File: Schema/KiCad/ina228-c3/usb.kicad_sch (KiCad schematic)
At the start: 17 parts, among them U5 CP2102N-Axx-xQFN28, U6 CA-IS3741HW, U7 USBLC6-2P6

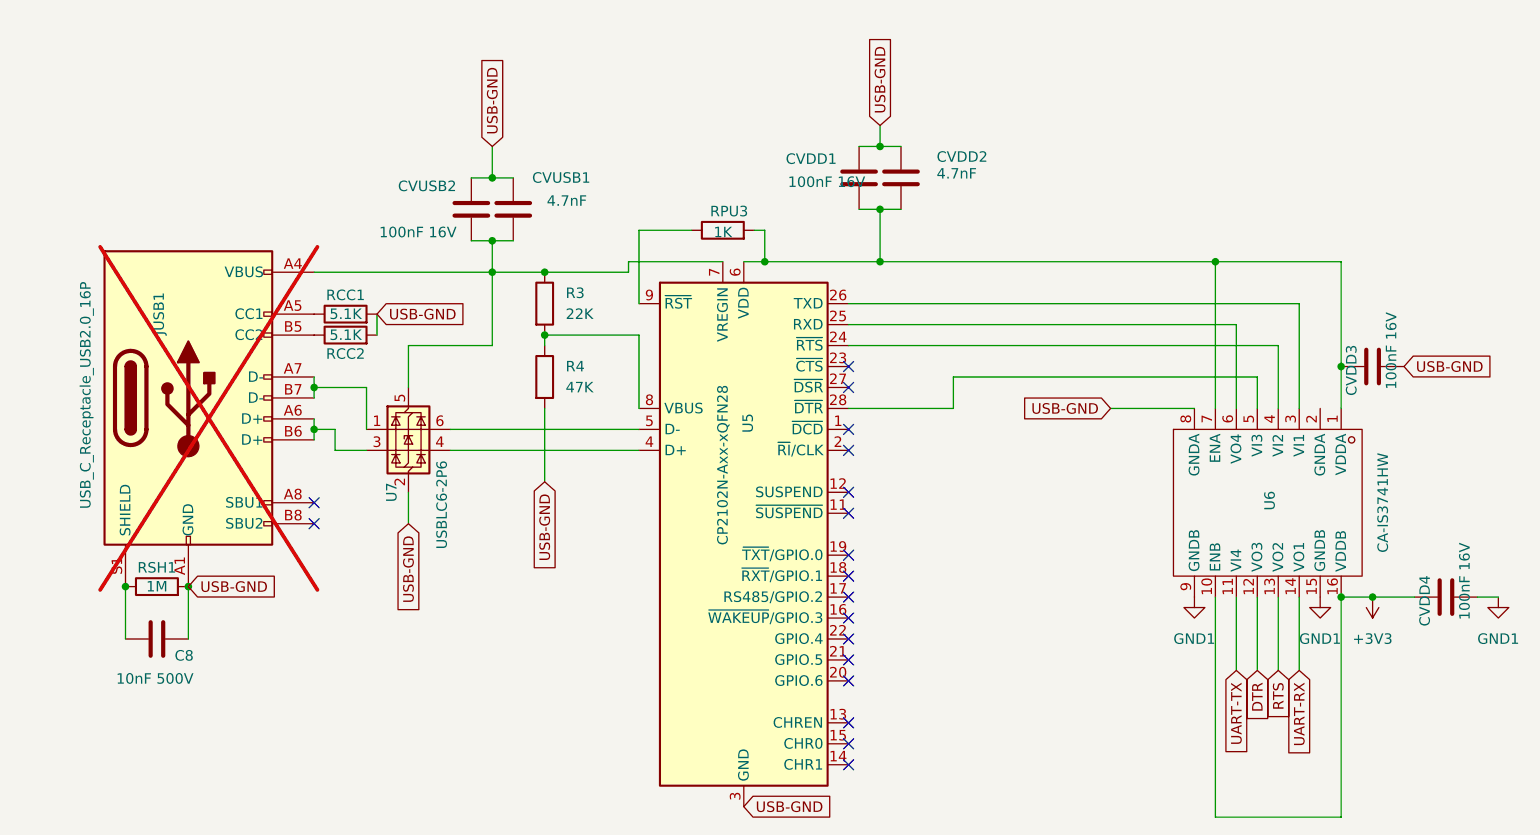
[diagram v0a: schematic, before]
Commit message: Remove usb2uart chip, making the design simpler (but probably more expensive.)
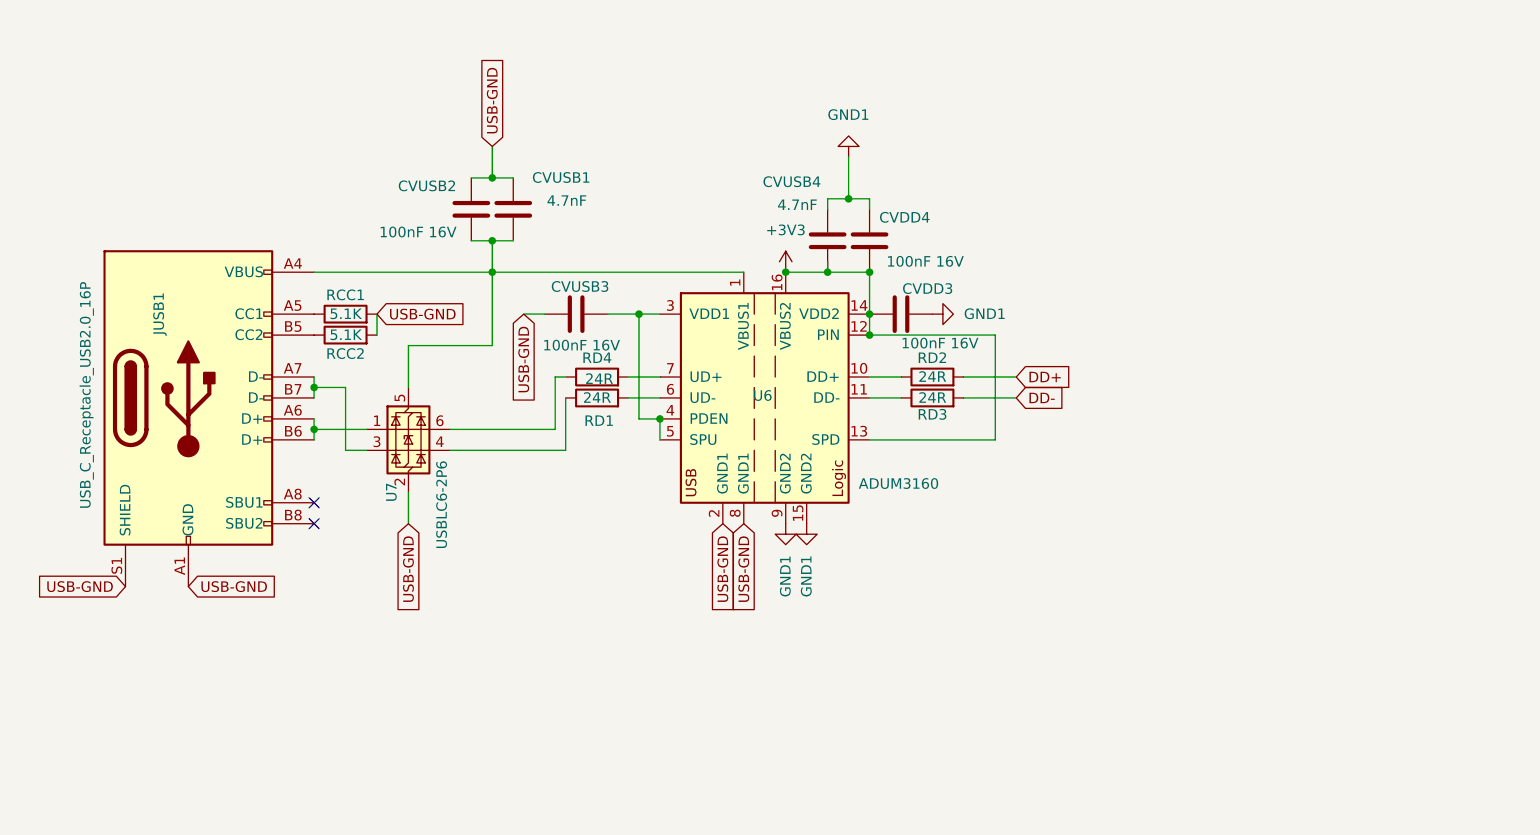
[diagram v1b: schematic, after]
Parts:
- removed C8: 10nF 500V, Capacitor_SMD:C_1206_3216Metric, symbol Device:C
- removed CVDD1: 100nF 16V, Capacitor_SMD:C_0603_1608Metric, symbol Device:C
- removed CVDD2: 4.7nF, Capacitor_SMD:C_0805_2012Metric, symbol Device:C
- removed R3: 22K, Resistor_SMD:R_0603_1608Metric, symbol Device:R
- removed R4: 47K, Resistor_SMD:R_0603_1608Metric, symbol Device:R
- removed RPU3: 1K, Resistor_SMD:R_0603_1608Metric, symbol Device:R
- removed RSH1: 1M, Resistor_SMD:R_0603_1608Metric, symbol Device:R
- removed U5: CP2102N-Axx-xQFN28, Package_DFN_QFN:QFN-28-1EP_5x5mm_P0.5mm_EP3.35x3.35mm, symbol Interface_USB:CP2102N-Axx-xQFN28
- added CVUSB3: 100nF 16V, Capacitor_SMD:C_0603_1608Metric, symbol Device:C
- added CVUSB4: 4.7nF, Capacitor_SMD:C_0805_2012Metric, symbol Device:C
- added RD1, RD2, RD3, RD4: 24R, Resistor_SMD:R_0603_1608Metric, symbol Device:R
- JUSB1: footprint easyeda:USB-C-SMD_TYPE-C16PIN -> Connector_USB:USB_C_Receptacle_Palconn_UTC16-G; now fitted
- U6: value CA-IS3741HW -> ADUM3160; symbol ProLib_pcs_2026-02-13:CA-IS3741HW -> Interface_USB:ADUM3160; LCSC C428890 -> C284149; LCSC Part Name CA-IS374x 高速四通道数字隔离器 -> (none); Supplier Part C428890 -> (none)
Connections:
- net DTR is gone; now on net +3V3: U6.12 (PIN)
- net RTS is gone; now on net +3V3: U6.13 (SPD)
- net UART-RX is gone; now on net +3V3: U6.14 (VDD2)
- net +3V3: now also CVDD3.1, CVUSB4.2; no longer U6.10 (ENB)
- net GND1: now also CVDD3.2, CVUSB4.1
- net USB-GND: now also JUSB1.S1 (SHIELD), U6.2 (GND1), CVUSB3.2; no longer CVDD3.2
- net at U6.3 (VDD1): now also U6.4 (PDEN), U6.5 (SPU), CVUSB3.1
- net at U6.6 (UD-): now also RD1.2
- net at CVUSB1.2, CVUSB2.2, JUSB1.A4 (VBUS)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: now also U6.1 (VBUS1)
- net at JUSB1.A7 (D-), JUSB1.B7 (D-): now also U7.3 (I/O2); no longer U7.1 (I/O1)
- net at JUSB1.A6 (D+), JUSB1.B6 (D+): now also U7.1 (I/O1); no longer U7.3 (I/O2)
- net at U7.4 (I/O2): now also RD1.1
- net at U7.6 (I/O1): now also RD4.1
- net UART-TX: no longer names the net of U6.11 (DD-)
- net UART-TX: now also RD3.1
- new net: RD2.1, U6.10 (DD+)
- new net: RD4.2, U6.7 (UD+)
- new net DD+: RD2.2
- new net DD-: RD3.2
- no-connect marks 18 -> 2
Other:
- moved on the sheet: CVDD3, CVDD4
